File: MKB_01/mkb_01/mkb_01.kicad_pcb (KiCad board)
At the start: 2 copper layers, 360 parts, among them J1 USB_C_Receptacle_USB2.0, J2 SW_Push, K1 SW_Push, M1 SW_Push, P1 SW_Push, Q1 SW_Push, Q2 BSP318, Q3 BSP318, T1 SW_Push, U1 LD1117S33TR_SOT223, U2 STM32F070CBTx, U3 SW_Push, X1 SW_Push, Y1 SW_Push, Y2 Crystal

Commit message: added FN key fixed layout
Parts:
- added D163: LED amber, LED_SMD:LED_0402_1005Metric_Pad0.77x0.64mm_HandSolder, F.Cu at (274.3, 158.0)
- added D164: 1N4148, Diode_SMD:D_0603_1608Metric_Pad1.05x0.95mm_HandSolder, B.Cu at (279.3, 158.0)
- added FN1: SW_Push, Button_Switch_Keyboard:SW_Cherry_MX_1.00u_PCB, F.Cu at (271.8, 168.9)
- added R91: 220, Resistor_SMD:R_0603_1608Metric_Pad0.98x0.95mm_HandSolder, B.Cu at (269.4, 158.0)
- LSHIFT1, PICDOWN1, SUPER1: footprint Button_Switch_Keyboard:SW_Cherry_MX_1.25u_PCB -> Button_Switch_Keyboard:SW_Cherry_MX_1.00u_PCB
- Q2, Q3: moved to B.Cu
- SHIFT1: footprint Button_Switch_Keyboard:SW_Cherry_MX_1.25u_PCB -> Button_Switch_Keyboard:SW_Cherry_MX_2.00u_PCB
- moved Y2 73.8 mm to (318.0, 62.3)
- moved Q3 65.0 mm to (338.9, 87.8), turned to 180 degrees
- moved Q2 63.0 mm to (305.1, 87.5)
- moved R3 55.6 mm to (320.6, 76.1), turned to 90 degrees
- moved U1 52.1 mm to (324.9, 73.4), turned to 270 degrees
- moved D2 50.3 mm to (320.6, 70.7), turned to 270 degrees
- moved C4 42.8 mm to (329.3, 74.0), turned to 90 degrees
- moved C1 42.2 mm to (329.3, 70.7), turned to 270 degrees
- moved D1 39.8 mm to (342.2, 70.3)
- moved JP1 27.4 mm to (333.6, 39.4)
- moved D53 14.3 mm to (260.0, 139.0)
- moved D58 14.3 mm to (279.0, 139.0)
- moved LINE1 14.3 mm to (290.8, 149.9)
- moved D28 14.3 mm to (183.8, 151.1)
- moved D33 14.3 mm to (202.8, 151.1)
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- renumbered Ä111 to Ä1111, Ö111 to Ö1111, Ü111 to Ü1111, ß111 to ß1111
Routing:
- net PA2: track 233.4 -> 320.4 mm
- net PA4: track 268.3 -> 341.4 mm
- net PB12: track 50.5 -> 118.9 mm
- net PA3: track 316.7 -> 340.4 mm
- net PB0: track 95.1 -> 109.8 mm
- net PB4: track 94.3 -> 108.8 mm
- net PB1: track 94.2 -> 108.6 mm
- net PB5: track 94.7 -> 109.0 mm
- net Net-(D164-Pad2): track 0.00 -> 8.53 mm
- net PB8: track 86.2 -> 80.4 mm
- net Net-(D67-Pad2): track 8.44 -> 3.81 mm
- net Net-(D62-Pad2): track 0.00 -> 3.70 mm
- net PB7: track 83.1 -> 80.4 mm
- net PB11: track 83.1 -> 80.4 mm
- net PB9: track 82.9 -> 80.3 mm
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
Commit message: changed quartz, finished placing and layers, some routing done
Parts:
- added H2: MountingHole, MountingHole:MountingHole_3.2mm_M3_DIN965_Pad_TopBottom, F.Cu at (74.3, 59.7)
- added H3: MountingHole, MountingHole:MountingHole_3.2mm_M3_DIN965_Pad_TopBottom, F.Cu at (77.9, 172.8)
- added H4: MountingHole, MountingHole:MountingHole_3.2mm_M3_DIN965_Pad_TopBottom, F.Cu at (340.9, 172.6)
- added H5: MountingHole, MountingHole:MountingHole_3.2mm_M3_DIN965_Pad_TopBottom, F.Cu at (341.0, 59.7)
- added H6: MountingHole, MountingHole:MountingHole_3.2mm_M3_DIN965_Pad_TopBottom, F.Cu at (207.6, 59.7)
- added H7: MountingHole, MountingHole:MountingHole_3.2mm_M3_DIN965_Pad_TopBottom, F.Cu at (207.6, 172.8)
- added H8: MountingHole, MountingHole:MountingHole_3.2mm_M3_DIN965_Pad_TopBottom, F.Cu at (140.9, 115.6)
- added H9: MountingHole, MountingHole:MountingHole_3.2mm_M3_DIN965_Pad_TopBottom, F.Cu at (274.3, 115.6)
- R11, R12, R13, R14, R15, R16, R18, R19, R20, R21, R22, R23, R24, R25, R26, R27, R28, R29, R30, R31, R32, R33, R35, R36, R37, R38, R39, R40, R41, R42, R43, R44, R45, R46, R47, R48, R49, R5, R50, R51, R52, R53, R54, R55, R56, R57, R58, R59, R6, R60, R61, R62, R63, R64, R65, R66, R67, R68, R69, R7, R70, R71, R72, R73, R74, R76, R77, R78, R79, R8, R80, R81, R82, R83, R84, R85, R86, R89, R9: moved to B.Cu
- Y2: footprint Crystal:Crystal_SMD_SeikoEpson_MA505-2Pin_12.7x5.1mm_HandSoldering -> Crystal:Crystal_SMD_Abracon_ABM3-2Pin_5.0x3.2mm_HandSoldering
- moved D126 321.9 mm to (83.9, 63.0), turned to 180 degrees
- moved D133 319.6 mm to (83.8, 82.0), turned to 180 degrees
- moved D110 318.5 mm to (67.0, 158.2), turned to 180 degrees
- moved D119 316.8 mm to (102.8, 63.0), turned to 180 degrees
- moved R53 309.2 mm to (78.8, 62.8)
- moved D82 305.4 mm to (93.2, 101.0), turned to 180 degrees
- moved D155 301.3 mm to (74.2, 139.2), turned to 180 degrees
- moved R9 297.5 mm to (88.4, 100.9)
- moved R37 296.1 mm to (62.2, 158.0)
- moved D135 294.6 mm to (102.8, 82.0), turned to 180 degrees
- moved R60 294.3 mm to (78.8, 81.8)
- moved R46 292.7 mm to (97.9, 62.8)
- moved D159 292.1 mm to (121.8, 63.0), turned to 180 degrees
- moved D93 290.0 mm to (121.8, 82.0), turned to 180 degrees
- moved D152 288.4 mm to (98.0, 120.0), turned to 180 degrees
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- renumbered LSHIFT1 to RSHIFT1, Ä1111 to Ä11111, Ö1111 to Ö11111, Ü1111 to Ü11111, ß1111 to ß11111
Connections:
- BACKSPACE1 pad 1: PA0 -> PA1
- C13 pad 2: Net-(C13-Pad2) -> 5V
- C18 pad 2: Net-(C13-Pad2) -> 5V
- D164 pad 1: PB12 -> PB11
- D33 pad 1: PB5 -> PB6
- D38 pad 1: PB6 -> PB5
- D63 pad 1: PB11 -> PB12
- D69 pad 1: PB14 -> PB13
- D70 pad 1: PB14 -> PB13
- D73 pad 1: PB15 -> PB14
- D76 pad 1: PB15 -> PB14
- D77 pad 1: PB15 -> PB14
- END1 pad 1: PA3 -> PA1
- ENTER1 pad 1: PA1 -> PA2
- PICDOWN1 pad 1: PA4 -> PA3
- PICUP1 pad 1: PA4 -> PA2
- POS1 pad 1: PA2 -> PA0
- R15 pad 1: Net-(C13-Pad2) -> 5V
- R21 pad 1: Net-(C13-Pad2) -> 5V
- R26 pad 1: Net-(C13-Pad2) -> 5V
- R31 pad 1: Net-(C13-Pad2) -> 5V
- R37 pad 1: Net-(C13-Pad2) -> 5V
- R42 pad 1: Net-(C13-Pad2) -> 5V
- R47 pad 1: Net-(C13-Pad2) -> 5V
- R52 pad 1: Net-(C13-Pad2) -> 5V
- R57 pad 1: Net-(C13-Pad2) -> 5V
- R62 pad 1: Net-(C13-Pad2) -> 5V
- R67 pad 1: Net-(C13-Pad2) -> 5V
- R72 pad 1: Net-(C13-Pad2) -> 5V
- R77 pad 1: Net-(C13-Pad2) -> 5V
- R82 pad 1: Net-(C13-Pad2) -> 5V
- R87 pad 1: Net-(C13-Pad2) -> 5V
- R9 pad 1: Net-(C13-Pad2) -> 5V
- RIGHT1 pad 1: PA3 -> PA4
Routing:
- net GND: track 0.00 -> 1211.0 mm, vias 0 -> 3
- net PB13: track 25.3 -> 90.6 mm
- net PB15: track 65.8 -> 19.6 mm
- net PA4: track 341.4 -> 298.4 mm
- net PB12: track 118.9 -> 86.5 mm
- net PA2: track 320.4 -> 349.2 mm
- net PB6: track 102.8 -> 75.8 mm, vias 2 -> 0
- net PB14: track 95.1 -> 68.6 mm
- net PA0: track 301.5 -> 277.5 mm
- net PA1: track 304.6 -> 327.3 mm
- net PA3: track 340.4 -> 317.8 mm
- net PB11: track 80.4 -> 102.0 mm
- net PB4: track 108.8 -> 90.9 mm
- net PB5: track 109.0 -> 97.5 mm
- net CAPS_LED_GND: track 0.00 -> 6.30 mm
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- added copper zone on F.Cu, net 3V3
- added copper zone on B.Cu, net 5V
- added copper zone on B.Cu, net GND
- added copper zone on F.Cu, net GND
- added copper zone on F.Cu, net LED_GND
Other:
- board outline added: 310 x 120 mm

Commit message: routing somewhat finished
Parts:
- moved C19 33.5 mm to (202.9, 135.2)
- moved C16 22.4 mm to (298.0, 153.3)
- moved C15 19.1 mm to (98.2, 160.0)
- moved C20 18.9 mm to (73.9, 135.3)
- moved C11 15.0 mm to (345.5, 135.5)
- moved C17 12.4 mm to (67.4, 97.2)
- moved C18 10.4 mm to (112.4, 68.3)
- moved C14 10.0 mm to (350.1, 97.0)
- moved JP1 9.27 mm to (333.1, 74.2)
- moved C13 4.73 mm to (263.9, 60.9)
- moved C5 4.27 mm to (312.4, 69.1), turned to 45 degrees
- moved R23 3.10 mm to (288.4, 62.8)
- moved R38 3.10 mm to (269.4, 62.8)
- moved C12 2.87 mm to (207.7, 67.0)
- moved C4 2.75 mm to (339.0, 66.9), turned to 180 degrees
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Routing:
- net LED_GND: track 0.00 -> 1716.3 mm, vias 0 -> 17
- net GND: track 1211.0 -> 96.8 mm, vias 3 -> 27
- net PB0: track 109.8 -> 551.6 mm, vias 0 -> 3
- net PC14: track 0.00 -> 349.2 mm, vias 0 -> 2
- net PC15: track 0.00 -> 342.0 mm, vias 0 -> 2
- net PA15: track 0.00 -> 335.2 mm, vias 0 -> 2
- net PA7: track 0.00 -> 305.9 mm, vias 0 -> 2
- net CAPS_LED_GND: track 6.30 -> 254.1 mm, vias 0 -> 1
- net PB3: track 91.1 -> 338.3 mm, vias 0 -> 2
- net PB1: track 108.6 -> 340.7 mm, vias 0 -> 2
- net PB4: track 90.9 -> 319.4 mm, vias 0 -> 2
- net PB2: track 90.5 -> 303.1 mm, vias 0 -> 2
- net PB5: track 97.5 -> 305.7 mm, vias 0 -> 2
- net PB6: track 75.8 -> 265.3 mm, vias 0 -> 2
- net PB7: track 80.4 -> 251.8 mm, vias 0 -> 2
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- added copper zone on B.Cu, net 3V3
- removed copper zone on F.Cu, net 3V3
- removed copper zone on B.Cu, net GND
- removed copper zone on F.Cu, net LED_GND

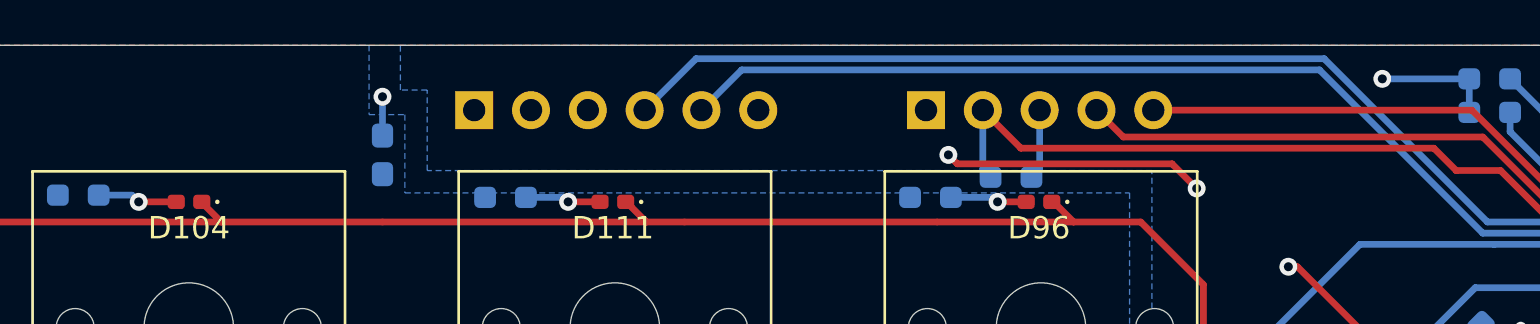
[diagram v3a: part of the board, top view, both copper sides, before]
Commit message: fixed silkscreen markings, exported and checked jlcpcb
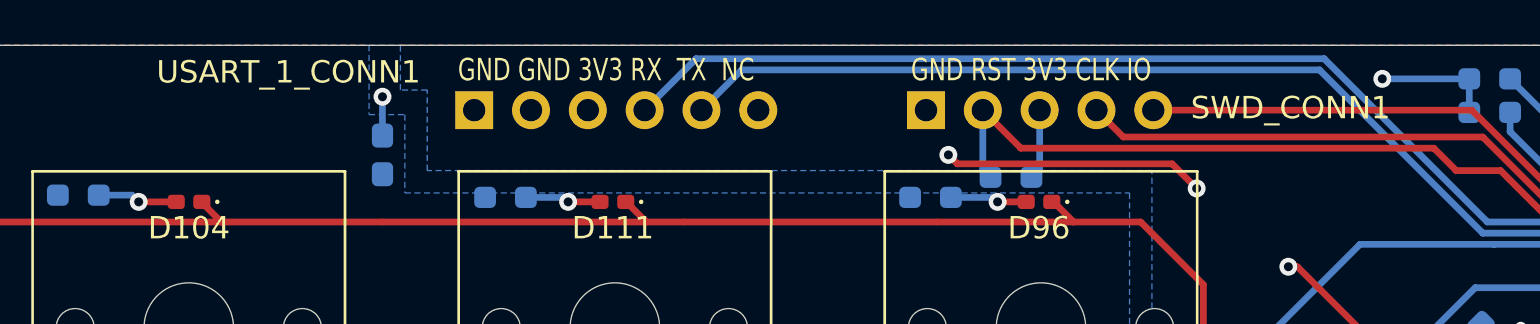
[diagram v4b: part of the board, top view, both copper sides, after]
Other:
- board text added: "3V3 BOOT0 GND"
- board text added: "GND GND 3V3 RX TX NC"
- board text added: "GND RST 3V3 CLK IO"
- board text added: "JLCJLCJLCJLC"

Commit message: added ferrit beads and optimized pcb a bit
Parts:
- added FB1: Ferrite_Bead_Small, Inductor_SMD:L_0603_1608Metric_Pad1.05x0.95mm_HandSolder, B.Cu at (330.0, 76.4)
- added FB2: Ferrite_Bead_Small, Inductor_SMD:L_0603_1608Metric_Pad1.05x0.95mm_HandSolder, B.Cu at (326.8, 66.3)
- added FB3: Ferrite_Bead_Small, Inductor_SMD:L_0603_1608Metric_Pad1.05x0.95mm_HandSolder, B.Cu at (331.9, 74.6)
- added FB4: Ferrite_Bead_Small, Inductor_SMD:L_0603_1608Metric_Pad1.05x0.95mm_HandSolder, B.Cu at (315.8, 83.0)
- added FB5: Ferrite_Bead_Small, Inductor_SMD:L_0603_1608Metric_Pad1.05x0.95mm_HandSolder, B.Cu at (312.2, 67.3)
- moved C7 17.7 mm to (316.4, 79.6), turned to 270 degrees
- moved C3 16.1 mm to (313.7, 67.3), turned to 270 degrees
- moved C5 15.0 mm to (326.8, 64.8), turned to 0 degrees
- moved C2 11.0 mm to (327.3, 76.1), turned to 0 degrees
- moved JP1 3.81 mm to (336.9, 73.9)
- moved C10 3.68 mm to (318.9, 83.4), turned to 180 degrees
- moved R57 1.80 mm to (325.0, 84.7)
- moved C6 1.51 mm to (329.4, 73.7), turned to 180 degrees
- renumbered Ä11111 to Ä1111111, Ö11111 to Ö1111111, Ü11111 to Ü1111111, ß11111 to ß1111111
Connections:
- C2 pad 1: 3V3 -> Net-(C2-Pad1)
- C3 pad 1: 3V3 -> Net-(C3-Pad1)
- C5 pad 1: 3V3 -> Net-(C5-Pad1)
- C6 pad 1: 3V3 -> Net-(C6-Pad1)
- C7 pad 1: 3V3 -> Net-(C7-Pad1)
- U2 pad 1: 3V3 -> Net-(C2-Pad1)
- U2 pad 24: 3V3 -> Net-(C3-Pad1)
- U2 pad 36: 3V3 -> Net-(C5-Pad1)
- U2 pad 48: 3V3 -> Net-(C6-Pad1)
- U2 pad 9: 3V3 -> Net-(C7-Pad1)
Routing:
- net PB0: track 551.6 -> 373.5 mm
- net 3V3: track 62.9 -> 105.1 mm, vias 13 -> 11
- net PA3: track 393.8 -> 410.5 mm
- net Net-(C7-Pad1): track 0.00 -> 12.0 mm
- net Net-(C2-Pad1): track 0.00 -> 7.93 mm
- net Net-(C6-Pad1): track 0.00 -> 7.61 mm
- net PB12: track 112.7 -> 119.7 mm
- net Net-(C3-Pad1): track 0.00 -> 5.19 mm
- net Net-(C5-Pad1): track 0.00 -> 4.10 mm
- net Net-(JP1-Pad2): track 9.15 -> 12.8 mm
- net PB13: track 142.9 -> 146.1 mm
- net Net-(D130-Pad2): track 6.80 -> 3.86 mm
- net LED_GND: track 1716.3 -> 1719.2 mm, vias 17 -> 15
- net PA7: track 305.9 -> 308.4 mm
- net BACK_LIGHT: track 29.9 -> 32.2 mm
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
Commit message: change diode direction to read from column rather than rows, added some more caps for the mcu, updated BOM
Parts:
- added C21: 10u, Capacitor_SMD:C_0603_1608Metric_Pad1.08x0.95mm_HandSolder, B.Cu at (308.0, 67.0)
- added C22: 10u, Capacitor_SMD:C_0603_1608Metric_Pad1.08x0.95mm_HandSolder, B.Cu at (308.0, 65.4)
- added C23: 10u, Capacitor_SMD:C_0603_1608Metric_Pad1.08x0.95mm_HandSolder, B.Cu at (308.0, 68.6)
- added C24: 10u, Capacitor_SMD:C_0603_1608Metric_Pad1.08x0.95mm_HandSolder, B.Cu at (308.0, 70.2)
- turned D10 to 0 degrees
- turned D11 to 0 degrees
- turned D12 to 0 degrees
- turned D13 to 0 degrees
- turned D14 to 0 degrees
- turned D15 to 0 degrees
- turned D16 to 0 degrees
- turned D164 to 0 degrees
- turned D17 to 180 degrees
- turned D19 to 0 degrees
- turned D20 to 0 degrees
- turned D21 to 0 degrees
- turned D22 to 0 degrees
- turned D23 to 180 degrees
- turned D24 to 0 degrees
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- renumbered Ä1111111 to Ä11111111, Ö1111111 to Ö11111111, Ü1111111 to Ü11111111, ß1111111 to ß11111111
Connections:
- D10 pad 1: PB1 -> Net-(D10-Pad1)
- D10 pad 2: Net-(D10-Pad2) -> PB1
- D11 pad 1: PB1 -> Net-(A1-Pad2)
- D11 pad 2: Net-(A1-Pad2) -> PB1
- D12 pad 1: PB1 -> Net-(D12-Pad1)
- D12 pad 2: Net-(D12-Pad2) -> PB1
- D13 pad 1: PB2 -> Net-(D13-Pad1)
- D13 pad 2: Net-(D13-Pad2) -> PB2
- D14 pad 1: PB2 -> Net-(D14-Pad1)
- D14 pad 2: Net-(D14-Pad2) -> PB2
- D15 pad 1: PB2 -> Net-(D15-Pad1)
- D15 pad 2: Net-(D15-Pad2) -> PB2
- D16 pad 1: PB2 -> Net-(D16-Pad1)
- D16 pad 2: Net-(D16-Pad2) -> PB2
- D164 pad 1: PB11 -> Net-(D164-Pad1)
- D164 pad 2: Net-(D164-Pad2) -> PB11
- D17 pad 1: PB2 -> Net-(D17-Pad1)
- D17 pad 2: Net-(D17-Pad2) -> PB2
- D19 pad 1: PB3 -> Net-(D19-Pad1)
- D19 pad 2: Net-(D19-Pad2) -> PB3
- D20 pad 1: PB3 -> Net-(D20-Pad1)
- D20 pad 2: Net-(D20-Pad2) -> PB3
- D21 pad 1: PB3 -> Net-(D21-Pad1)
- D21 pad 2: Net-(D21-Pad2) -> PB3
- D22 pad 1: PB3 -> Net-(D18-Pad2)
- D22 pad 2: Net-(D18-Pad2) -> PB3
- D23 pad 1: PB3 -> Net-(C8-Pad2)
- D23 pad 2: Net-(C8-Pad2) -> PB3
- D24 pad 1: PB4 -> Net-(D24-Pad1)
- D24 pad 2: Net-(D24-Pad2) -> PB4
- D25 pad 1: PB4 -> Net-(D25-Pad1)
- D25 pad 2: Net-(D25-Pad2) -> PB4
- D26 pad 1: PB4 -> Net-(D26-Pad1)
- D26 pad 2: Net-(D26-Pad2) -> PB4
- D27 pad 1: PB4 -> Net-(D27-Pad1)
- D27 pad 2: Net-(D27-Pad2) -> PB4
- D28 pad 1: PB4 -> Net-(D28-Pad1)
- D28 pad 2: Net-(D28-Pad2) -> PB4
- D29 pad 1: PB5 -> Net-(D29-Pad1)
- D29 pad 2: Net-(D29-Pad2) -> PB5
- D3 pad 1: PB0 -> Net-(D3-Pad1)
- D3 pad 2: Net-(D3-Pad2) -> PB0
- D30 pad 1: PB5 -> Net-(D30-Pad1)
- D30 pad 2: Net-(D30-Pad2) -> PB5
- D31 pad 1: PB5 -> Net-(D31-Pad1)
- D31 pad 2: Net-(D31-Pad2) -> PB5
- D32 pad 1: PB5 -> Net-(D32-Pad1)
- D32 pad 2: Net-(D32-Pad2) -> PB5
- D33 pad 1: PB6 -> Net-(B1-Pad2)
- D33 pad 2: Net-(B1-Pad2) -> PB6
- D34 pad 1: PB6 -> Net-(D34-Pad1)
- D34 pad 2: Net-(D34-Pad2) -> PB6
- D35 pad 1: PB6 -> Net-(D35-Pad1)
- D35 pad 2: Net-(D35-Pad2) -> PB6
- D36 pad 1: PB6 -> Net-(D36-Pad1)
- D36 pad 2: Net-(D36-Pad2) -> PB6
- D37 pad 1: PB6 -> Net-(D37-Pad1)
- D37 pad 2: Net-(D37-Pad2) -> PB6
- D38 pad 1: PB5 -> Net-(D38-Pad1)
- D38 pad 2: Net-(D38-Pad2) -> PB5
- D39 pad 1: PB7 -> Net-(D39-Pad1)
- D39 pad 2: Net-(D39-Pad2) -> PB7
- D4 pad 1: PB0 -> Net-(D4-Pad1)
- D4 pad 2: Net-(D4-Pad2) -> PB0
- D40 pad 1: PB7 -> Net-(D40-Pad1)
- D40 pad 2: Net-(D40-Pad2) -> PB7
- D41 pad 1: PB7 -> Net-(D41-Pad1)
- D41 pad 2: Net-(D41-Pad2) -> PB7
- D42 pad 1: PB7 -> Net-(D42-Pad1)
- D42 pad 2: Net-(D42-Pad2) -> PB7
- D43 pad 1: PB7 -> Net-(D43-Pad1)
- D43 pad 2: Net-(D43-Pad2) -> PB7
- D44 pad 1: PB8 -> Net-(D44-Pad1)
- D44 pad 2: Net-(D44-Pad2) -> PB8
- D45 pad 1: PB8 -> Net-(D45-Pad1)
- D45 pad 2: Net-(D45-Pad2) -> PB8
- D46 pad 1: PB8 -> Net-(D46-Pad1)
- D46 pad 2: Net-(D46-Pad2) -> PB8
- D47 pad 1: PB8 -> Net-(D47-Pad1)
- D47 pad 2: Net-(D47-Pad2) -> PB8
- D48 pad 1: PB8 -> Net-(D48-Pad1)
- D48 pad 2: Net-(D48-Pad2) -> PB8
- D49 pad 1: PB9 -> Net-(D49-Pad1)
- D49 pad 2: Net-(D49-Pad2) -> PB9
- D5 pad 1: PB0 -> Net-(D5-Pad1)
- D5 pad 2: Net-(D5-Pad2) -> PB0
- D50 pad 1: PB9 -> Net-(D50-Pad1)
- D50 pad 2: Net-(D50-Pad2) -> PB9
- D51 pad 1: PB9 -> Net-(D51-Pad1)
- D51 pad 2: Net-(D51-Pad2) -> PB9
- D52 pad 1: PB9 -> Net-(D52-Pad1)
- D52 pad 2: Net-(D52-Pad2) -> PB9
- D53 pad 1: PB9 -> Net-(COMMA1-Pad2)
- D53 pad 2: Net-(COMMA1-Pad2) -> PB9
- D54 pad 1: PB10 -> Net-(D54-Pad1)
- D54 pad 2: Net-(D54-Pad2) -> PB10
- D55 pad 1: PB10 -> Net-(D55-Pad1)
- D55 pad 2: Net-(D55-Pad2) -> PB10
- D56 pad 1: PB10 -> Net-(D56-Pad1)
- D56 pad 2: Net-(D56-Pad2) -> PB10
- D57 pad 1: PB10 -> Net-(D57-Pad1)
- D57 pad 2: Net-(D57-Pad2) -> PB10
- D58 pad 1: PB10 -> Net-(D58-Pad1)
- D58 pad 2: Net-(D58-Pad2) -> PB10
- D59 pad 1: PB11 -> Net-(D59-Pad1)
- D59 pad 2: Net-(D59-Pad2) -> PB11
- D6 pad 1: PB0 -> Net-(CAPS1-Pad2)
- D6 pad 2: Net-(CAPS1-Pad2) -> PB0
- D60 pad 1: PB11 -> Net-(D60-Pad1)
- D60 pad 2: Net-(D60-Pad2) -> PB11
- D61 pad 1: PB11 -> Net-(D61-Pad1)
- D61 pad 2: Net-(D61-Pad2) -> PB11
- D62 pad 1: PB11 -> Net-(D62-Pad1)
- D62 pad 2: Net-(D62-Pad2) -> PB11
- D63 pad 1: PB12 -> Net-(D63-Pad1)
- D63 pad 2: Net-(D63-Pad2) -> PB12
- D64 pad 1: PB12 -> Net-(D64-Pad1)
- D64 pad 2: Net-(D64-Pad2) -> PB12
- D65 pad 1: PB12 -> Net-(BACKSLASH1-Pad2)
- D65 pad 2: Net-(BACKSLASH1-Pad2) -> PB12
- D66 pad 1: PB12 -> Net-(D66-Pad1)
- D66 pad 2: Net-(D66-Pad2) -> PB12
- D67 pad 1: PB12 -> Net-(D67-Pad1)
- D67 pad 2: Net-(D67-Pad2) -> PB12
- D68 pad 1: PB15 -> Net-(D68-Pad1)
- D68 pad 2: Net-(D68-Pad2) -> PB15
- D69 pad 1: PB13 -> Net-(BACKSPACE1-Pad2)
- D69 pad 2: Net-(BACKSPACE1-Pad2) -> PB13
- D7 pad 1: PB0 -> Net-(D7-Pad1)
- D7 pad 2: Net-(D7-Pad2) -> PB0
- D70 pad 1: PB13 -> Net-(D70-Pad1)
- D70 pad 2: Net-(D70-Pad2) -> PB13
- D71 pad 1: PB13 -> Net-(D71-Pad1)
- D71 pad 2: Net-(D71-Pad2) -> PB13
- D72 pad 1: PB15 -> Net-(D72-Pad1)
- D72 pad 2: Net-(D72-Pad2) -> PB15
- D73 pad 1: PB14 -> Net-(D73-Pad1)
- D73 pad 2: Net-(D73-Pad2) -> PB14
- D74 pad 1: PB14 -> Net-(D74-Pad1)
- D74 pad 2: Net-(D74-Pad2) -> PB14
- D75 pad 1: PB13 -> Net-(D75-Pad1)
- D75 pad 2: Net-(D75-Pad2) -> PB13
- D76 pad 1: PB14 -> Net-(D76-Pad1)
- D76 pad 2: Net-(D76-Pad2) -> PB14
- D77 pad 1: PB14 -> Net-(D77-Pad1)
- D77 pad 2: Net-(D77-Pad2) -> PB14
- D78 pad 1: PB14 -> Net-(D78-Pad1)
- D78 pad 2: Net-(D78-Pad2) -> PB14
- D79 pad 1: PB13 -> Net-(D79-Pad1)
- D79 pad 2: Net-(D79-Pad2) -> PB13
- D8 pad 1: PB1 -> Net-(D8-Pad1)
- D8 pad 2: Net-(D8-Pad2) -> PB1
- D9 pad 1: PB1 -> Net-(D9-Pad1)
- D9 pad 2: Net-(D9-Pad2) -> PB1
- DEL1 pad 2: Net-(D68-Pad2) -> Net-(D68-Pad1)
- DOWN1 pad 2: Net-(D75-Pad2) -> Net-(D75-Pad1)
- E1 pad 2: Net-(D21-Pad2) -> Net-(D21-Pad1)
- EIGHT1 pad 2: Net-(D45-Pad2) -> Net-(D45-Pad1)
- END1 pad 2: Net-(D73-Pad2) -> Net-(D73-Pad1)
- ENTER1 pad 2: Net-(D70-Pad2) -> Net-(D70-Pad1)
- ESC1 pad 2: Net-(D3-Pad2) -> Net-(D3-Pad1)
- F1 pad 2: Net-(D8-Pad2) -> Net-(D8-Pad1)
- F10 pad 2: Net-(D54-Pad2) -> Net-(D54-Pad1)
- F11 pad 2: Net-(D59-Pad2) -> Net-(D59-Pad1)
- F12 pad 2: Net-(D64-Pad2) -> Net-(D64-Pad1)
- F13 pad 2: Net-(D27-Pad2) -> Net-(D27-Pad1)
- F2 pad 2: Net-(D13-Pad2) -> Net-(D13-Pad1)
- F3 pad 2: Net-(D19-Pad2) -> Net-(D19-Pad1)
- F4 pad 2: Net-(D24-Pad2) -> Net-(D24-Pad1)
- F5 pad 2: Net-(D29-Pad2) -> Net-(D29-Pad1)
- F6 pad 2: Net-(D34-Pad2) -> Net-(D34-Pad1)
- F7 pad 2: Net-(D39-Pad2) -> Net-(D39-Pad1)
- F8 pad 2: Net-(D44-Pad2) -> Net-(D44-Pad1)
- F9 pad 2: Net-(D49-Pad2) -> Net-(D49-Pad1)
- FIVE1 pad 2: Net-(D30-Pad2) -> Net-(D30-Pad1)
- FN1 pad 2: Net-(D164-Pad2) -> Net-(D164-Pad1)
- FOUR1 pad 2: Net-(D25-Pad2) -> Net-(D25-Pad1)
- G1 pad 2: Net-(D32-Pad2) -> Net-(D32-Pad1)
- GREATER1 pad 2: Net-(D7-Pad2) -> Net-(D7-Pad1)
- H1 pad 2: Net-(D37-Pad2) -> Net-(D37-Pad1)
- HASH1 pad 2: Net-(D67-Pad2) -> Net-(D67-Pad1)
- I1 pad 2: Net-(D46-Pad2) -> Net-(D46-Pad1)
- J2 pad 2: Net-(D42-Pad2) -> Net-(D42-Pad1)
- K1 pad 2: Net-(D47-Pad2) -> Net-(D47-Pad1)
- L1 pad 2: Net-(D52-Pad2) -> Net-(D52-Pad1)
- LEFT1 pad 2: Net-(D79-Pad2) -> Net-(D79-Pad1)
- LINE1 pad 2: Net-(D63-Pad2) -> Net-(D63-Pad1)
- M1 pad 2: Net-(D48-Pad2) -> Net-(D48-Pad1)
- N1 pad 2: Net-(D43-Pad2) -> Net-(D43-Pad1)
- NINE1 pad 2: Net-(D50-Pad2) -> Net-(D50-Pad1)
- O1 pad 2: Net-(D51-Pad2) -> Net-(D51-Pad1)
- ONE1 pad 2: Net-(D9-Pad2) -> Net-(D9-Pad1)
- P1 pad 2: Net-(D56-Pad2) -> Net-(D56-Pad1)
- PICDOWN1 pad 2: Net-(D78-Pad2) -> Net-(D78-Pad1)
- PICUP1 pad 2: Net-(D77-Pad2) -> Net-(D77-Pad1)
- PLUS1 pad 2: Net-(D66-Pad2) -> Net-(D66-Pad1)
- POINT1 pad 2: Net-(D58-Pad2) -> Net-(D58-Pad1)
- POS1 pad 2: Net-(D76-Pad2) -> Net-(D76-Pad1)
- PRINT1 pad 2: Net-(D72-Pad2) -> Net-(D72-Pad1)
- Q1 pad 2: Net-(D10-Pad2) -> Net-(D10-Pad1)
- R4 pad 2: Net-(D26-Pad2) -> Net-(D26-Pad1)
- RIGHT1 pad 2: Net-(D74-Pad2) -> Net-(D74-Pad1)
- S1 pad 2: Net-(D16-Pad2) -> Net-(D16-Pad1)
- SEVEN1 pad 2: Net-(D40-Pad2) -> Net-(D40-Pad1)
- SIX1 pad 2: Net-(D35-Pad2) -> Net-(D35-Pad1)
- SPACE1 pad 2: Net-(D38-Pad2) -> Net-(D38-Pad1)
- T1 pad 2: Net-(D31-Pad2) -> Net-(D31-Pad1)
- TAB1 pad 2: Net-(D5-Pad2) -> Net-(D5-Pad1)
- THREE1 pad 2: Net-(D20-Pad2) -> Net-(D20-Pad1)
- TWO1 pad 2: Net-(D14-Pad2) -> Net-(D14-Pad1)
- U3 pad 2: Net-(D41-Pad2) -> Net-(D41-Pad1)
- UP1 pad 2: Net-(D71-Pad2) -> Net-(D71-Pad1)
- V1 pad 2: Net-(D28-Pad2) -> Net-(D28-Pad1)
- W1 pad 2: Net-(D15-Pad2) -> Net-(D15-Pad1)
- X1 pad 2: Net-(D17-Pad2) -> Net-(D17-Pad1)
- Y1 pad 2: Net-(D12-Pad2) -> Net-(D12-Pad1)
- Z1 pad 2: Net-(D36-Pad2) -> Net-(D36-Pad1)
- ZERO1 pad 2: Net-(D55-Pad2) -> Net-(D55-Pad1)
- ^1 pad 2: Net-(D4-Pad2) -> Net-(D4-Pad1)
- Ä11111111 pad 2: Net-(D62-Pad2) -> Net-(D62-Pad1)
- Ö11111111 pad 2: Net-(D57-Pad2) -> Net-(D57-Pad1)
- Ü11111111 pad 2: Net-(D61-Pad2) -> Net-(D61-Pad1)
- ß11111111 pad 2: Net-(D60-Pad2) -> Net-(D60-Pad1)
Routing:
- net Net-(D164-Pad2): track 8.53 -> 0.00 mm
- net Net-(D164-Pad1): track 0.00 -> 8.53 mm
- net Net-(D38-Pad2): track 8.52 -> 0.00 mm
- net Net-(D38-Pad1): track 0.00 -> 8.52 mm
- net Net-(D74-Pad2): track 8.50 -> 0.00 mm
- net Net-(D74-Pad1): track 0.00 -> 8.50 mm
- net Net-(D17-Pad2): track 8.49 -> 0.00 mm
- net Net-(D17-Pad1): track 0.00 -> 8.49 mm
- net Net-(D79-Pad2): track 8.43 -> 0.00 mm
- net Net-(D79-Pad1): track 0.00 -> 8.43 mm
- net Net-(D78-Pad2): track 8.42 -> 0.00 mm
- net Net-(D78-Pad1): track 0.00 -> 8.42 mm
- net Net-(D75-Pad2): track 8.41 -> 0.00 mm
- net Net-(D75-Pad1): track 0.00 -> 8.41 mm
- net Net-(D48-Pad2): track 8.40 -> 0.00 mm
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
